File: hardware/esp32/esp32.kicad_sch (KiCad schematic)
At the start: 149 parts, among them J1 PlugIn_Terminal_Screw, J2 ESP_left, J3 ESP_right, J4 PlugIn_Terminal_01x02, Q4 MMBT5401, Q5 MMBT2222A, U5 ES8374, U5 LMV321, U6 LM393, U6 LMV321, U7 AMS1117-3.3

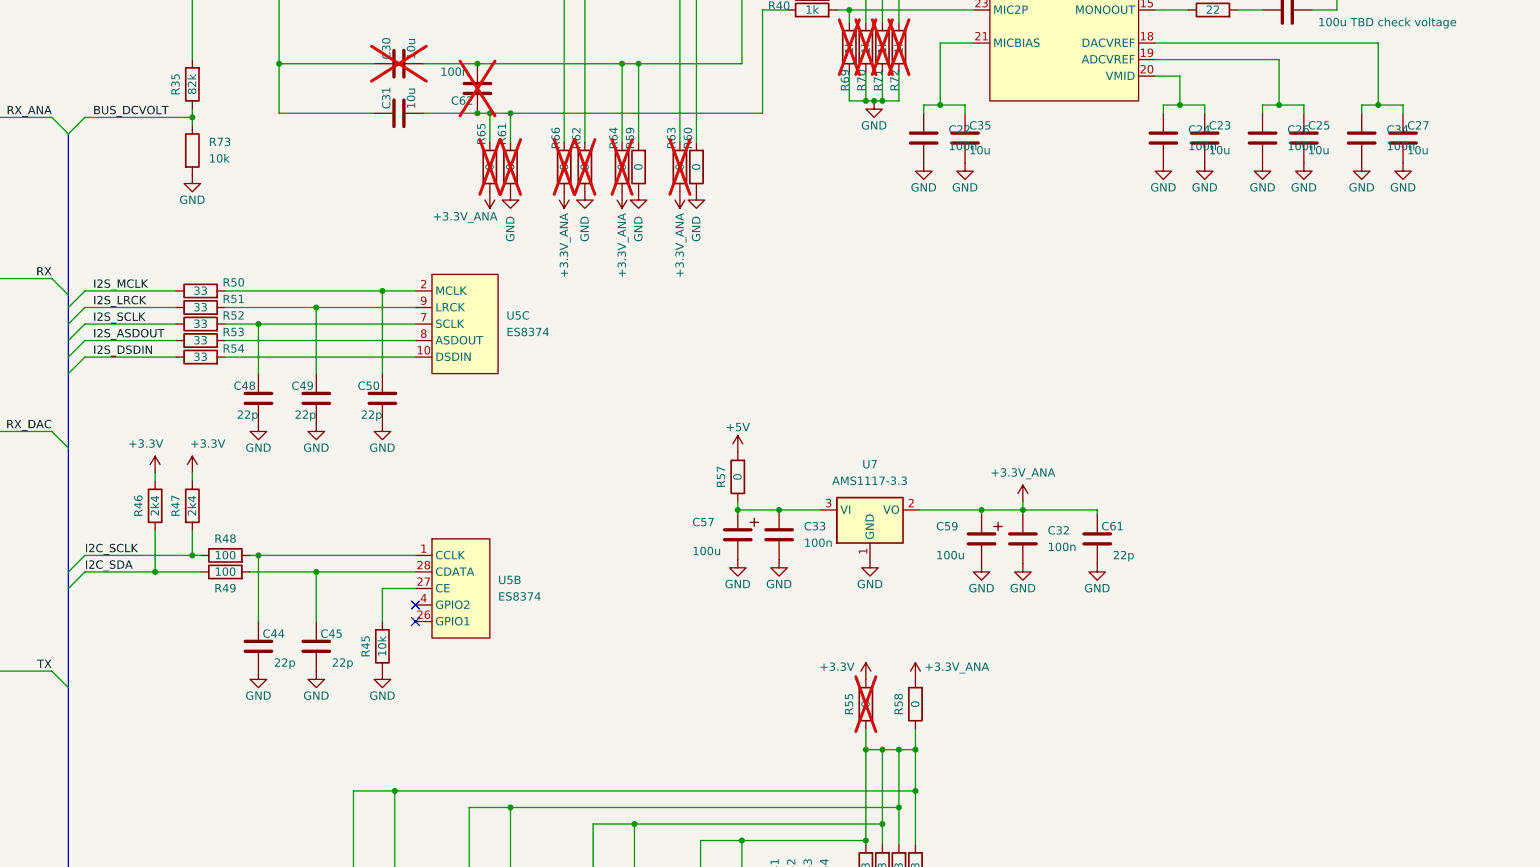
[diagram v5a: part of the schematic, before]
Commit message: First layout with DRC check on V4.0
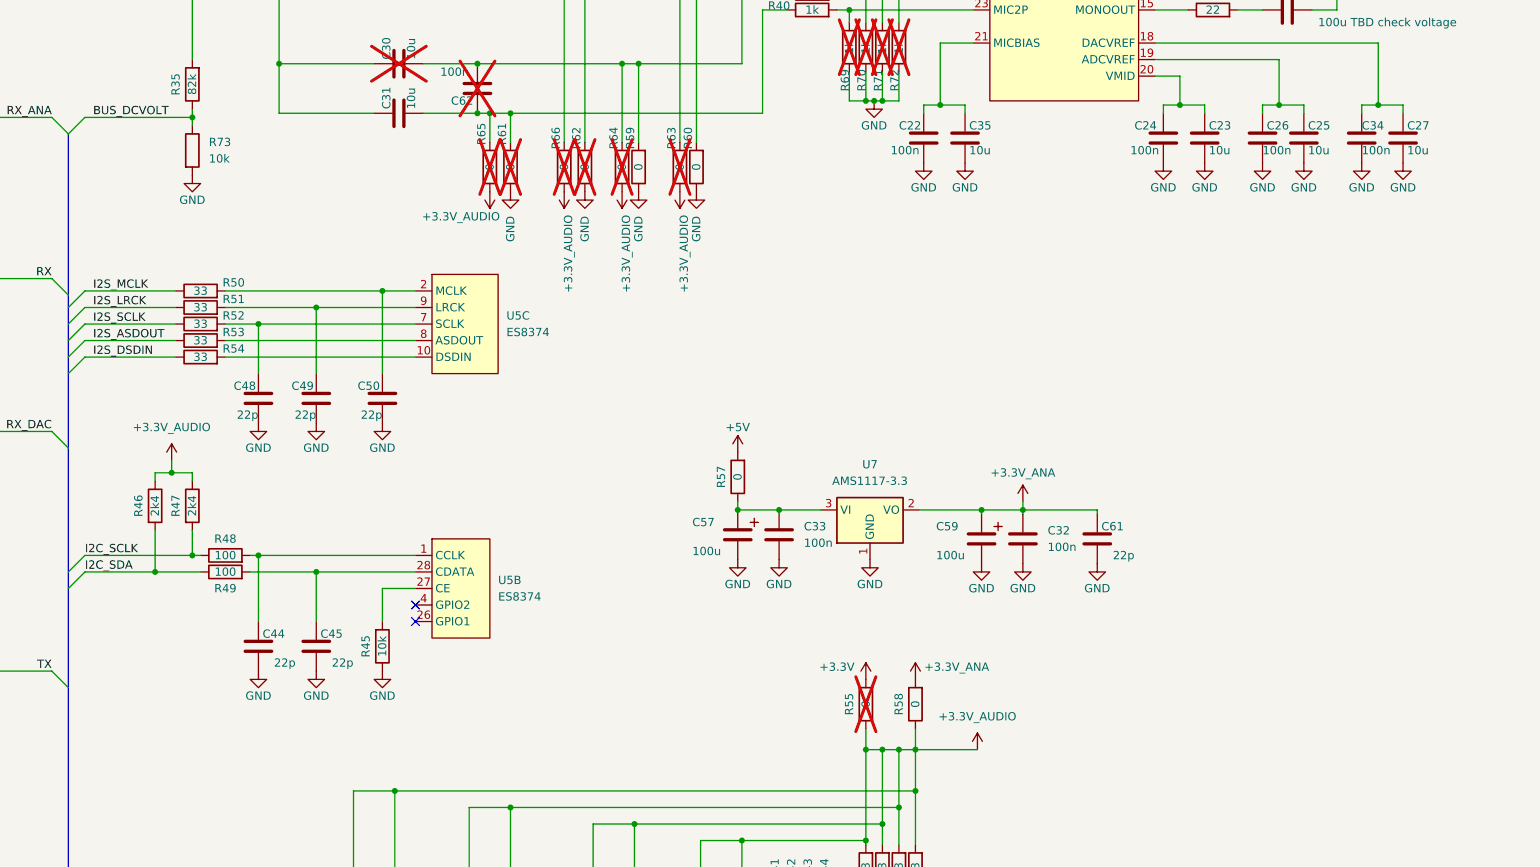
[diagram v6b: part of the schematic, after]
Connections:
- net +3.3V: no longer R46.1, R47.1
- net +3.3V_ANA: no longer R63.1, R64.1, R65.1, R66.1
- net +3.3V_AUDIO: now reaches C46.2, C47.2, C51.2, C52.2, C53.2, C54.2, C55.2, C56.2, R41.2, R42.2, R43.2, R44.2, R55.1, R58.1
- net +3.3V_AUDIO: now also R46.1, R47.1, R63.1, R64.1, R65.1, R66.1

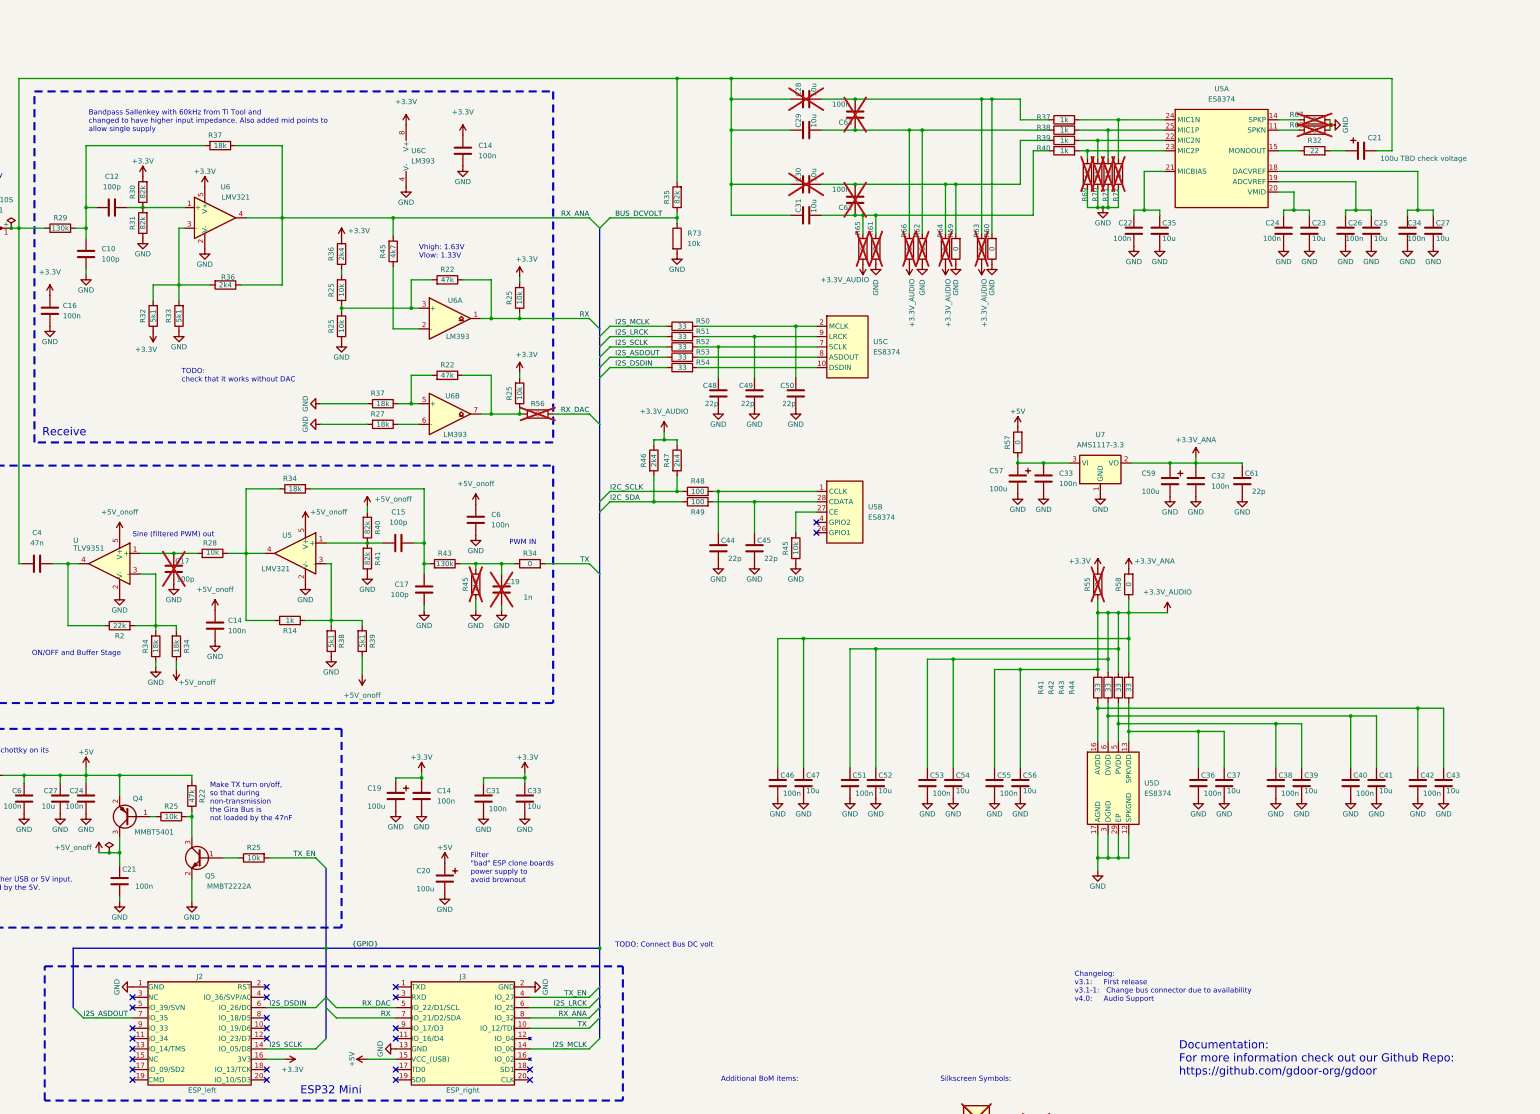
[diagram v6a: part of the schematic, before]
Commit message: Add production data for first audio try (v4.0)
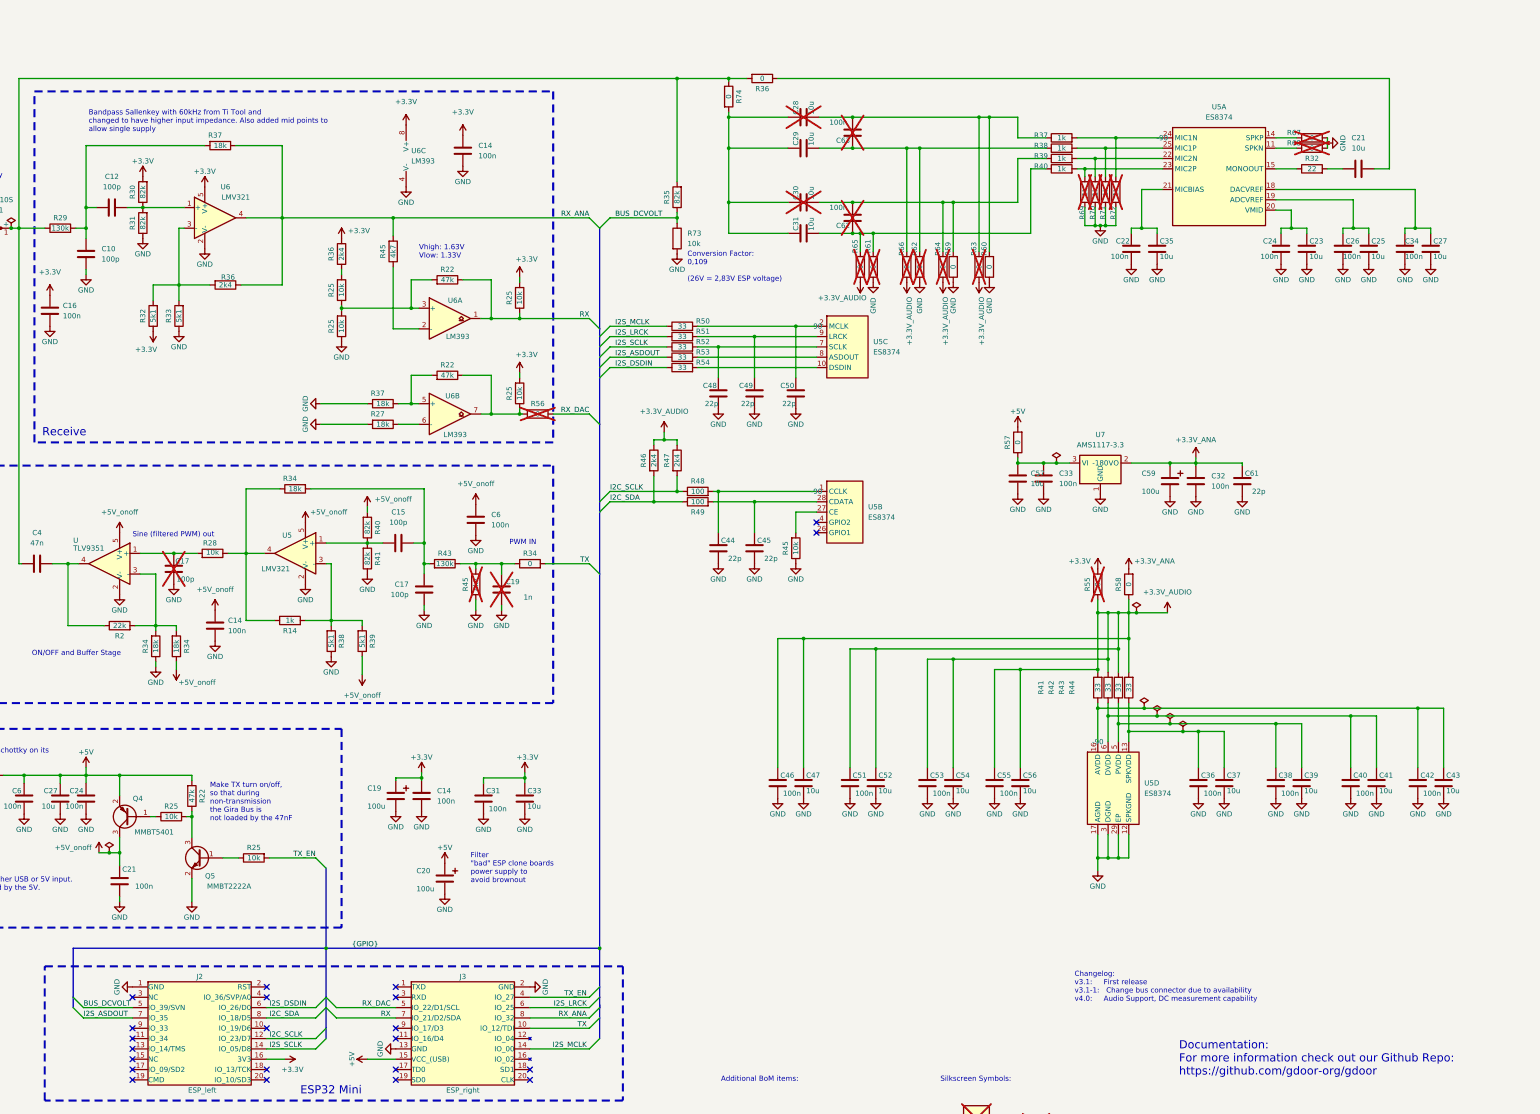
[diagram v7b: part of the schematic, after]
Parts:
- removed C21: 100u TBD check voltage, Library:C_1210_3225Metric_Pad1.33x2.70mm_HandSolder, symbol symbols:100u
- removed C57: 100u, Library:C_1210_3225Metric_Pad1.33x2.70mm_HandSolder, symbol symbols:100u
- added C21, C57: 10u, Library:C_1206_3216Metric_Pad1.33x1.80mm_HandSolder, symbol symbols:10u_1206
- added R36, R74: 0, Library:R_0603_1608Metric_Pad0.98x0.95mm_HandSolder, symbol symbols:0R
- U5: footprint Library:QFN-28-1EP_4x4mm_P0.4mm_EP2.3x2.3mm -> Library:QFN-28-1EP_4x4mm_P0.45mm_EP2.4x2.4mm; JlcRotOffset (none) -> -90
- U7: JlcRotOffset (none) -> -180
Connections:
- net BUS_DCVOLT: now also J2.5 (IO_39/SVN)
- net GND: now also C57.1
- net I2C_SCLK: now also J2.12 (IO_23/D7)
- net I2C_SDA: now also J2.8 (IO_18/D5)
- net at C28.2, C29.2, C30.2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: now also R74.2; no longer C4.2, D1.1 (+), R29.1, R35.2
- net at C33.1, R57.1, U7.3 (VI): now also C57.2
- net at R32.2: now also C21.1
- new net: C4.2, D1.1 (+), R29.1, R35.2, R36.2, R74.1
- new net: C21.2, R36.1
- no-connect marks 25 -> 22
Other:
- note added: "Changelog: v3.1: First release v3.1-1: Change bus connector due to availability v4.0: Audio Support, DC measurement capability"
- note added: "Conversion Factor: 0,109 (26V = 2,83V ESP voltage)"
- note removed: "Changelog: v3.1: First release v3.1-1: Change bus connector due to availability v4.0: Audio Support"
- note removed: "TODO: Connect Bus DC volt"
- note removed: "TODO: check that it works without DAC"
- moved on the sheet: C22, C23, C24, C25, C26, C27, C28, C29, C30, C31, C34, C35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

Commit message: Start with V4.1, which includes ESP32-S3
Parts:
- removed J2: ESP_left, Library:PinHeader_2x10_P2.54mm_Vertical, symbol symbols:ESP_left
- removed J3: ESP_right, Library:PinHeader_2x10_P2.54mm_Vertical, symbol symbols:ESP_right
- removed U4: ~, Library:ESP32_mini_no_pads, symbol symbols:ESPSilkscreen
- added U4: ~, Library:ESP32-S3-DEVKITC-1-N8R2, symbol symbols:ESP32-S3-DEVKITC-SYMBOL
- added U8: ESP32-S3-DEVKITC-1-N8R2_LEFT, Library:PinHeader_1x22_P2.54mm_Vertical, symbol symbols:ESP32-S3-DEVKITC-1-N8R2_LEFT
- added U9: ESP32-S3-DEVKITC-1-N8R2, Library:PinHeader_1x22_P2.54mm_Vertical, symbol symbols:ESP32-S3-DEVKITC-1-N8R2_RIGHT
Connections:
- no-connect marks 22 -> 2
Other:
- note added: "Changelog: v3.1: First release v3.1-1: Change bus connector due to availability v4.0: Audio Support, DC measurement capability v4.1: Adapt to ESP32-S3 board"
- note added: "ESP32 S3 Dev Board"
- note removed: "Changelog: v3.1: First release v3.1-1: Change bus connector due to availability v4.0: Audio Support, DC measurement capability"
- note removed: "ESP32 Footprint and Symbol thanks to https://github.com/r0oland/ESP32_mini_KiCad_Library"
- note removed: "ESP32 Mini"
- moved on the sheet: C32, C33, C36, C37, C38, C39, C40, C41, C42, C43, C46, C47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
